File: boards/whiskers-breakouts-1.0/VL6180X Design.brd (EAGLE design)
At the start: 72.5 x 21 mm, 25 parts, among them J2 6-PIN_2MM-V, Q3 BSS138, Q4 BSS138, U1 VL6180X, U2 TLV74128PDBVR, U3 VL6180X, U4 VL6180X, U5 MIC5225-3.3YM5-TR

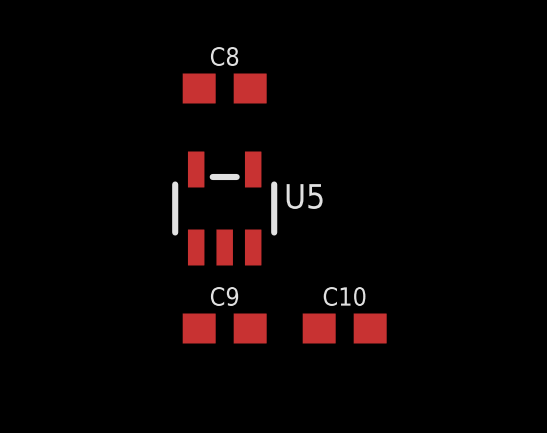
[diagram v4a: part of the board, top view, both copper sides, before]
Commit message: Update VL6180X Design.brd
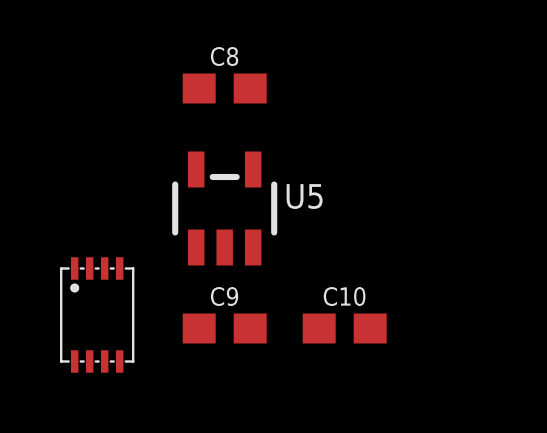
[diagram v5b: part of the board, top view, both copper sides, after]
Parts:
- added U$12: TXB0102DCUT, RoboJackets-ICs:S-PDSO-G8
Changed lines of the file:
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@@
 <attribute name="VALUE" x="9" y="-4.762" size="0.6096" layer="27" font="vector" ratio="20" align="top-center"/>
 </element>
+<element name="U$12" library="RoboJackets-ICs" package="S-PDSO-G8" value="TXB0102DCUT" x="1" y="-4" smashed="yes"/>
 </elements>
 <signals>

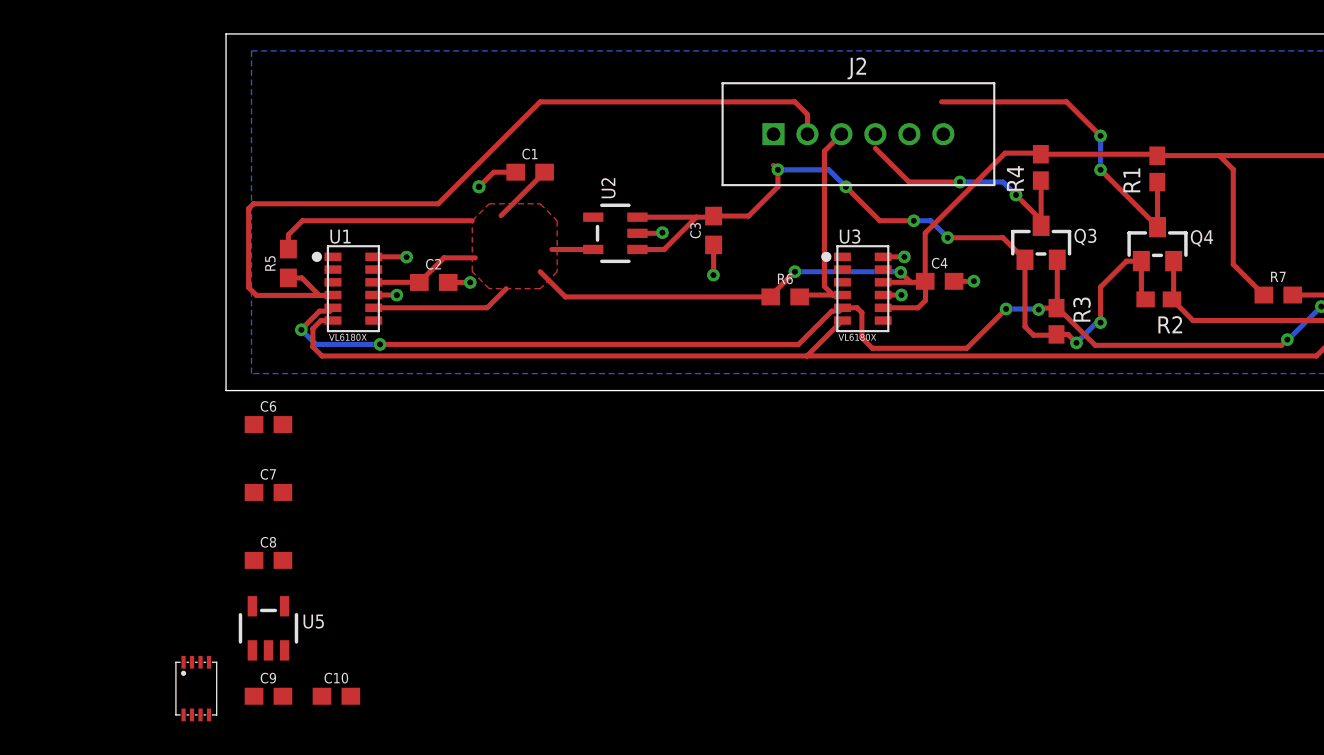
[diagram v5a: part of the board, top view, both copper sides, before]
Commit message: Corrected Schematic
This should complete the corrected schematic. Big Changes Include a BiDirectional Level Shifter IC instead of our old bi directional level shifter and two voltage regulators to ensure compatibility with control board.
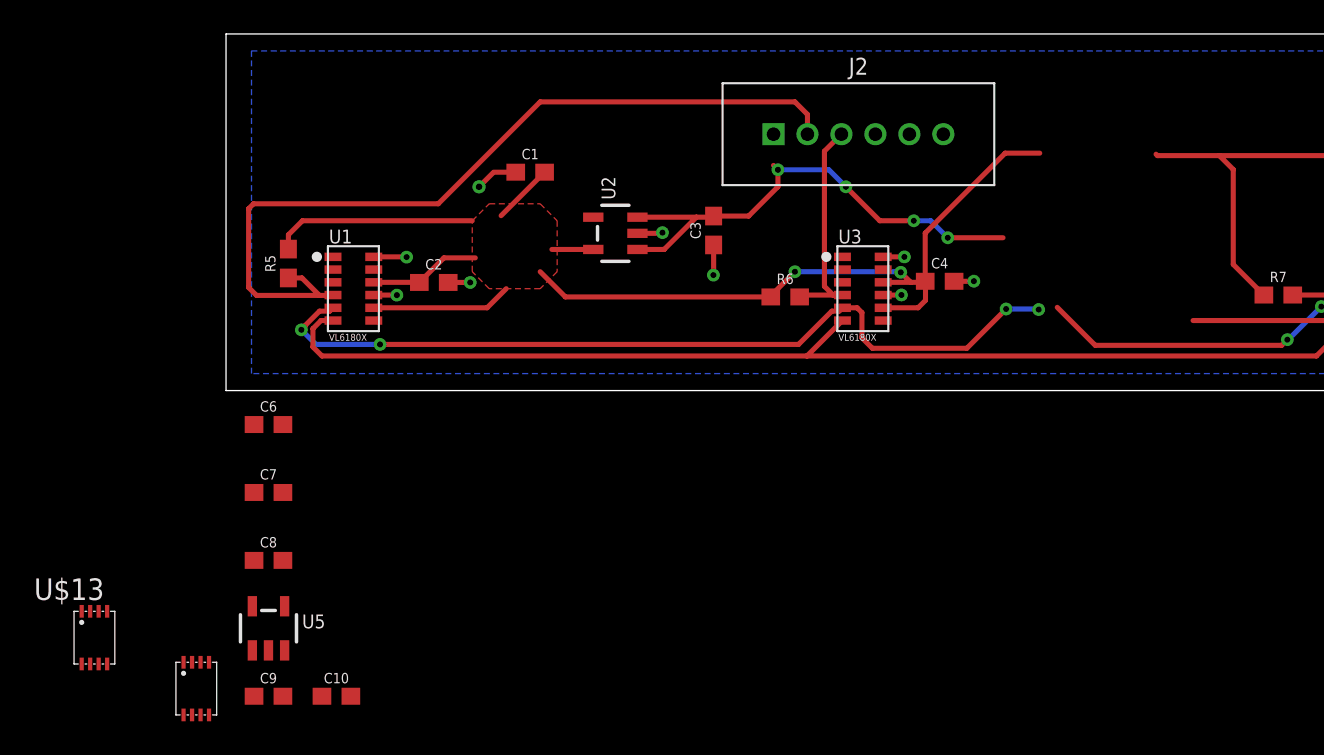
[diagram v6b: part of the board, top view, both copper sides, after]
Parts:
- removed Q3, Q4: BSS138, microbuilder:SOT23-WIDE
- removed R1, R2, R3, R4: 4.7k, RoboJackets-Resistors:R0603W
- added U$13: TXB0102DCUT, RoboJackets-ICs:S-PDSO-G8
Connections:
- net +3.3V: no longer Q3.1, Q4.1, R2.2, R3.2
- net SCL_2.8V: no longer Q3.2, R3.1
- net SCL_3.3V: no longer Q3.3, R4.1
- net SDA_2.8V: no longer Q4.2, R2.1
- net SDA_3.3V: no longer Q4.3, R1.1
- net VCC: no longer R1.2, R4.2
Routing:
- net SDA_3.3V: track 19.4 -> 0.00 mm, vias 2 -> 0
- net +3.3V: track 48.3 -> 29.6 mm, vias 6 -> 4
- net SCL_3.3V: track 14.5 -> 0.00 mm, vias 2 -> 0
- net VCC: track 122.9 -> 116.0 mm
- net SDA_2.8V: track 81.1 -> 77.0 mm
- net SCL_2.8V: track 73.1 -> 69.3 mm

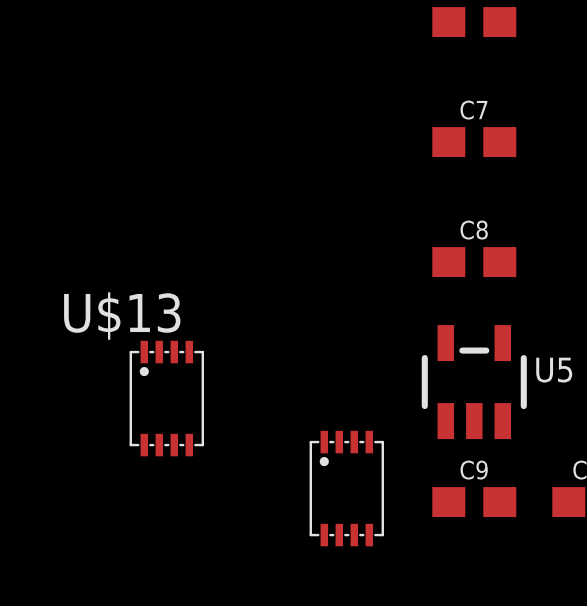
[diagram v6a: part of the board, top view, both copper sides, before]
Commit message: Update VL6180X Design.brd
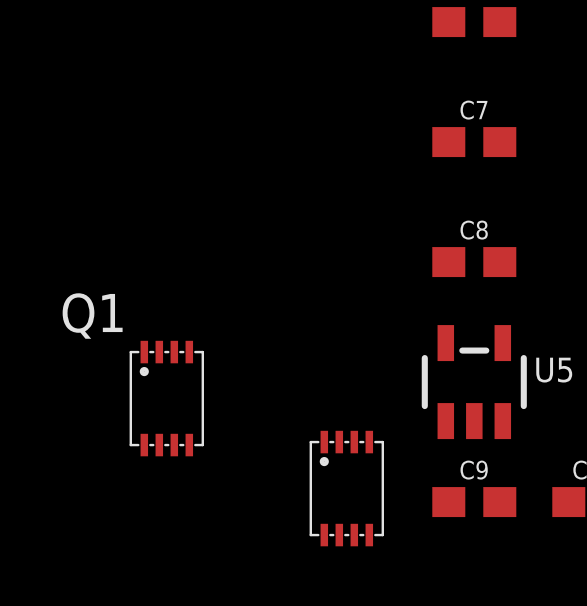
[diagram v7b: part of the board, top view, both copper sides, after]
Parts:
- Q1: value TXB0102DCUT -> (none)
- renumbered U$13 to Q1
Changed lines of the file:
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@@
 </element>
 <element name="U$12" library="RoboJackets-ICs" package="S-PDSO-G8" value="TXB0102DCUT" x="1" y="-4" smashed="yes"/>
-<element name="U$13" library="RoboJackets-ICs" package="S-PDSO-G8" value="TXB0102DCUT" x="-5" y="-1" smashed="yes">
+<element name="Q1" library="RoboJackets-ICs" package="S-PDSO-G8" value="" x="-5" y="-1" smashed="yes">
 <attribute name="NAME" x="-8.81" y="1.667" size="1.27" layer="25"/>
 <attribute name="VALUE" x="-8.556" y="-4.302" size="1.27" layer="27"/>

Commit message: Board Revisions
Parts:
- removed R5, R6, R7: 47k, SparkFun-Resistors:0603
- removed U$12: TXB0102DCUT, RoboJackets-ICs:S-PDSO-G8
- added R1: 1k, SparkFun-Resistors:0603
- added R2, R3, R4: 47k, SparkFun-Resistors:0603
- Q1: value (none) -> TXB0102DCU; device RoboJackets-ICs:S-PDSO-G8 -> RoboJackets-ICs:VFSOP-8
- moved C6 100.7 mm to (100.5, 44.0)
- moved C7 74.4 mm to (70.3, 43.7)
- moved Q1 73.0 mm to (50.1, 46.8), turned to 180 degrees
- moved C10 72.0 mm to (47.5, 56.8), turned to 270 degrees
- moved U5 67.2 mm to (47.7, 52.0), turned to 180 degrees
- moved C9 65.2 mm to (45.5, 47.1), turned to 90 degrees
- moved C8 53.6 mm to (40.0, 44.6)
- moved J2 47.2 mm to (79.1, 53.4)
- moved C5 41.3 mm to (100.5, 46.7), turned to 0 degrees
- moved C3 40.3 mm to (53.7, 56.9), turned to 270 degrees
- moved U2 40.2 mm to (53.4, 52.0), turned to 180 degrees
- moved C1 39.8 mm to (54.3, 47.8), turned to 90 degrees
- moved C4 36.8 mm to (70.3, 46.7)
- moved C2 36.4 mm to (40.0, 46.7)
- moved U1 36.1 mm to (35.0, 46.0)
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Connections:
- new net N$1: Q1.6, R1.1
- net +3.3V: now also Q1.7
- net GND: now also Q1.2, R1.2
- net RST_1: now also R2.1; no longer R5.1
- net RST_2: now also R3.2; no longer R6.2
- net RST_3: now also R4.2; no longer R7.2
- net SCL_2.8V: now also Q1.5
- net SCL_3.3V: now also Q1.8
- net SDA_2.8V: now also Q1.4
- net SDA_3.3V: now also Q1.1
- net VCC: now also Q1.3, R2.2, R3.1, R4.1; no longer R5.2, R6.1, R7.1
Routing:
- net SDA_2.8V: track 77.0 -> 0.00 mm
- net SCL_2.8V: track 69.3 -> 0.00 mm, vias 6 -> 0
- net VCC: track 116.0 -> 70.0 mm, vias 2 -> 0
- net RST_1: track 49.0 -> 3.18 mm
- net +5V: track 0.00 -> 40.1 mm
- net +3.3V: track 29.6 -> 16.6 mm, vias 4 -> 0
- net GND: track 18.3 -> 30.9 mm, vias 12 -> 9
- net RST_2: track 13.2 -> 3.74 mm
- removed copper zone on layer 1, net VCC
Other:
- board size 72.5 x 21 mm -> 81 x 23 mm
